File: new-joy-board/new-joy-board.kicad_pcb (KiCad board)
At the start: 2 copper layers, 95.2 x 83.8 mm, 33 parts, among them J0 SDS-50J, J1 SDS-50J, J2 SDS-50J, J3 SDS-50J, J4 BAT, U4 AZReady_ESP32, U5 dc_dc_converter, U6 AZ1117-3.3, U7 MPU6050_Breakout

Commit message: More PCB work to determine final dimensions for case construction
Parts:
- removed C1: 10uF, Capacitor_SMD:C_1210_3225Metric_Pad1.42x2.65mm_HandSolder
- removed C2: 100nF, Capacitor_SMD:C_1210_3225Metric_Pad1.42x2.65mm_HandSolder
- removed U6: AZ1117-3.3, Package_TO_SOT_SMD:SOT-223
- added U0: P82B715, new-joy:P82B715D, F.Cu at (90.2, 144.8)
- added U1: P82B715, new-joy:P82B715D, F.Cu at (90.2, 116.8)
- added U2: P82B715, new-joy:P82B715D, F.Cu at (138.4, 115.6)
- added U3: P82B715, new-joy:P82B715D, F.Cu at (135.9, 146.1)
- moved R9 133.2 mm to (139.5, 154.9)
- moved R10 125.4 mm to (138.4, 136.9), turned to 270 degrees
- moved R5 93.5 mm to (87.0, 123.9)
- moved R11 88.4 mm to (139.5, 123.2)
- moved R12 80.7 mm to (140.8, 106.7)
- moved R4 80.6 mm to (130.6, 106.7)
- moved R13 77.5 mm to (90.0, 106.7)
- moved R14 72.4 mm to (93.8, 125.7)
- moved R6 63.6 mm to (95.0, 109.2)
- moved R2 16.7 mm to (133.1, 137.2)
- moved R3 9.49 mm to (131.1, 123.5)
- moved R1 1.95 mm to (133.3, 155.2), turned to 90 degrees
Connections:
- R10 pad 2: /SDA3ESP -> /SDA3BUF
- U4 pad 1: Net-(U4-Pad1) -> +3V3
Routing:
- net +5V: track 42.3 -> 3.24 mm
- net +3V3: track 27.0 -> 10.7 mm
- net GND: track 7.77 -> 0.00 mm

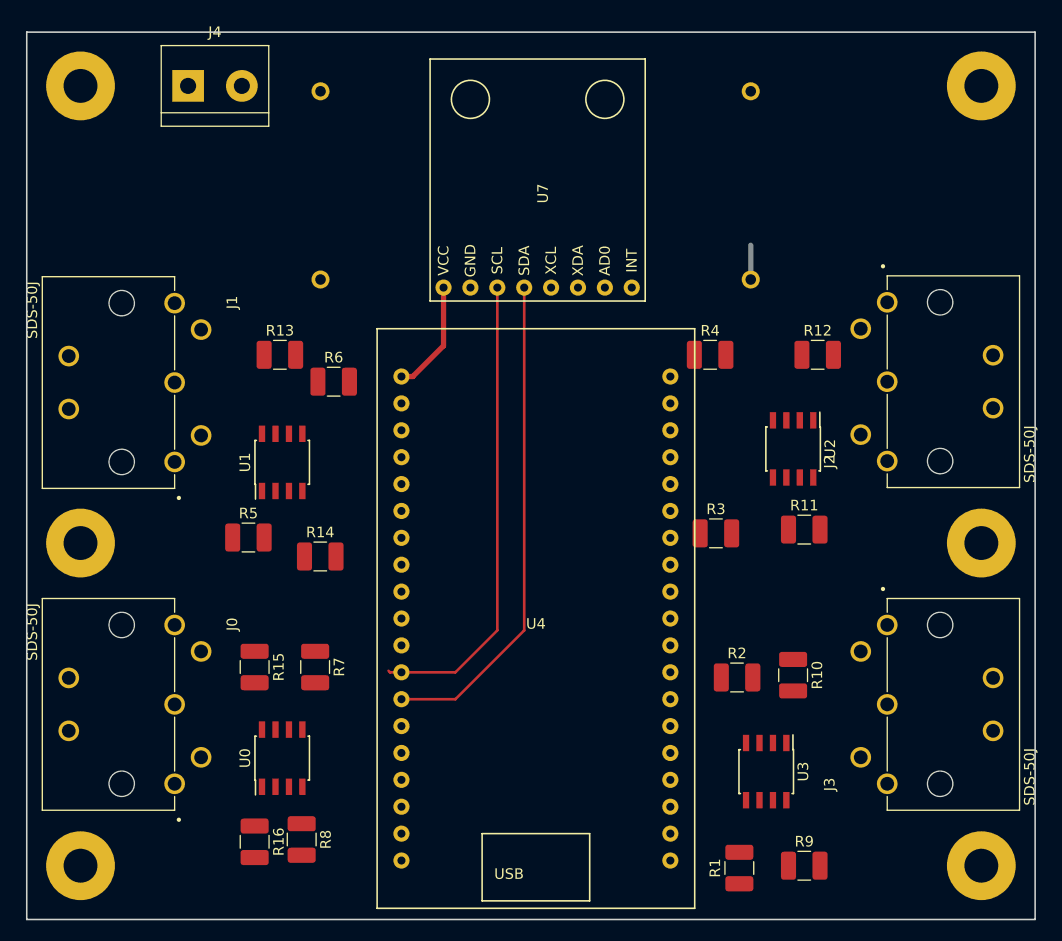
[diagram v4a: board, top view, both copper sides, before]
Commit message: Routet half of the I2C buffers
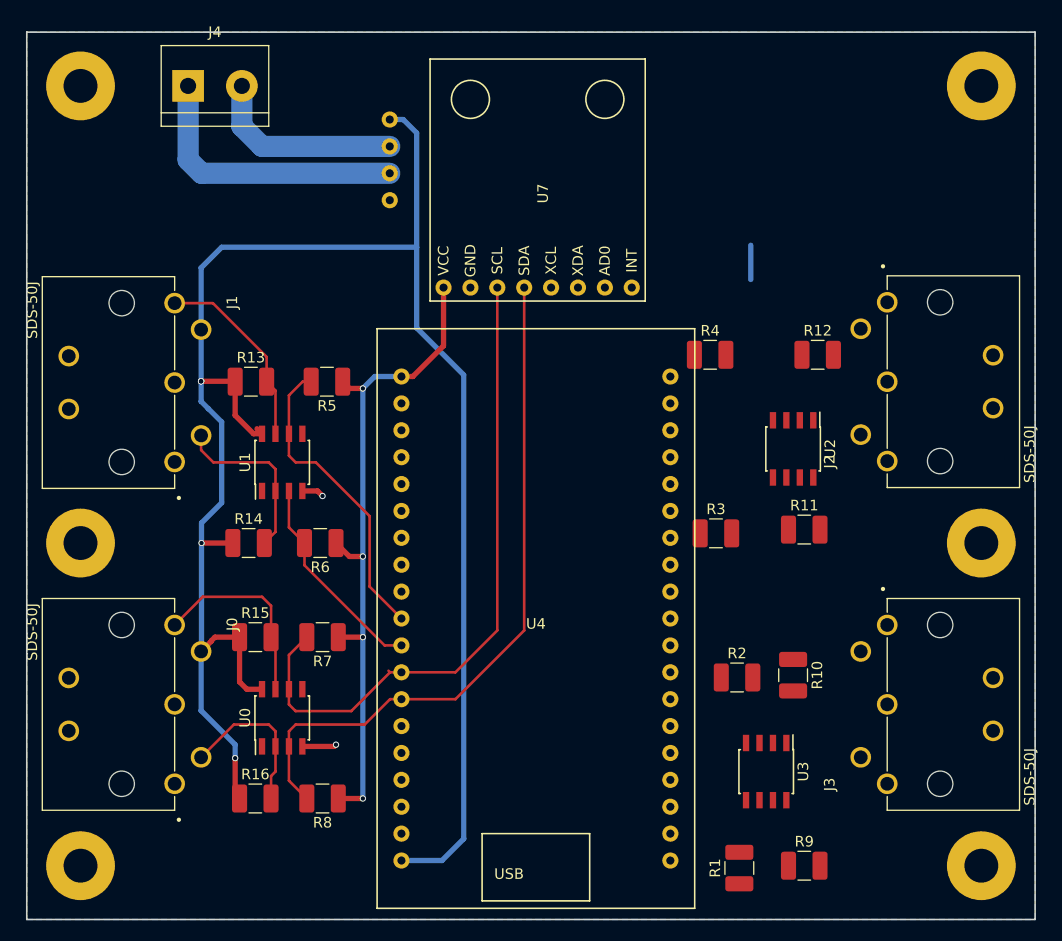
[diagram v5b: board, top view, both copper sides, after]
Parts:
- removed U5: dc_dc_converter, new-joy:dc_dc_converter
- added U10: oskj-dc-dc, new-joy:oskj-dc-dc, B.Cu at (109.2, 88.3)
- moved R5 16.5 mm to (94.4, 109.2), turned to 180 degrees
- moved R6 15.3 mm to (93.8, 124.5), turned to 180 degrees
- moved R14 6.89 mm to (87.0, 124.5)
- moved R8 4.34 mm to (94.0, 148.6), turned to 180 degrees
- moved R16 4.09 mm to (87.6, 148.6), turned to 0 degrees
- moved U0 3.81 mm to (90.2, 141.0)
- moved R13 3.74 mm to (87.2, 109.2)
- moved R7 2.91 mm to (94.0, 133.3), turned to 180 degrees
- moved R15 2.82 mm to (87.6, 133.3), turned to 0 degrees
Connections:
- J0 pad 1: GND -> -BATT
- J1 pad 1: GND -> -BATT
- J2 pad 1: GND -> -BATT
- J3 pad 1: GND -> -BATT
- J4 pad 2: +BATT -> -BATT
- U0 pad 4: GND -> -BATT
- U1 pad 4: GND -> -BATT
- U2 pad 4: GND -> -BATT
- U3 pad 4: GND -> -BATT
- U4 pad 32: GND -> -BATT
- U4 pad 38: GND -> -BATT
- U7 pad 2: GND -> -BATT
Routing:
- net +5V: track 3.24 -> 180.1 mm, vias 0 -> 4
- net +3V3: track 10.7 -> 63.4 mm, vias 0 -> 4
- net /SCL1ESP: track 0.00 -> 29.2 mm
- net +BATT: track 0.00 -> 26.6 mm
- net -BATT: track 0.00 -> 23.9 mm, vias 0 -> 2
- net /SDA1ESP: track 0.00 -> 19.9 mm
- net /SDA0ESP: track 46.7 -> 65.6 mm
- net /SCL0BUF: track 0.00 -> 18.6 mm
- net /SCL1BUF: track 0.00 -> 18.4 mm
- net /SCL0ESP: track 44.4 -> 62.7 mm
- net /SDA1BUF: track 0.00 -> 16.6 mm
- net /SDA0BUF: track 0.00 -> 15.1 mm
- added copper zone on B.Cu, net -BATT

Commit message: First draft of full layout
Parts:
- moved R1 3.39 mm to (133.3, 151.8), turned to 0 degrees
- moved R9 3.18 mm to (139.7, 151.8), turned to 180 degrees
- moved R4 2.83 mm to (133.3, 107.3)
- moved R3 2.42 mm to (133.3, 122.6)
- moved U2 2.01 mm to (136.5, 114.9)
- moved U3 1.86 mm to (136.5, 144.3)
- moved R10 1.29 mm to (139.7, 137.2), turned to 180 degrees
- moved R11 1.06 mm to (140.3, 122.6), turned to 180 degrees
- moved R12 0.76 mm to (140.3, 107.3), turned to 180 degrees
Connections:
- J0 pad S1: Net-(J0-PadS1) -> -BATT
- J0 pad S2: Net-(J0-PadS1) -> -BATT
- J1 pad S1: Net-(J1-PadS1) -> -BATT
- J1 pad S2: Net-(J1-PadS1) -> -BATT
- J2 pad S1: Net-(J2-PadS1) -> -BATT
- J2 pad S2: Net-(J2-PadS1) -> -BATT
- J3 pad S1: Net-(J3-PadS1) -> -BATT
- J3 pad S2: Net-(J3-PadS1) -> -BATT
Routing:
- net +5V: track 180.1 -> 285.5 mm, vias 4 -> 11
- net +3V3: track 63.4 -> 143.7 mm, vias 4 -> 8
- net /SDA2ESP: track 0.00 -> 33.8 mm
- net /SDA2BUF: track 0.00 -> 23.2 mm
- net /SCL2ESP: track 0.00 -> 22.8 mm
- net /SCL2BUF: track 0.00 -> 17.9 mm
- net /SCL3ESP: track 0.00 -> 17.7 mm
- net /SDA3ESP: track 0.00 -> 17.7 mm
- net /SCL3BUF: track 0.00 -> 17.6 mm
- net /SDA3BUF: track 0.00 -> 13.9 mm
- net -BATT: track 23.9 -> 26.5 mm, vias 2 -> 4
- net /SCL1ESP: track 29.2 -> 31.7 mm

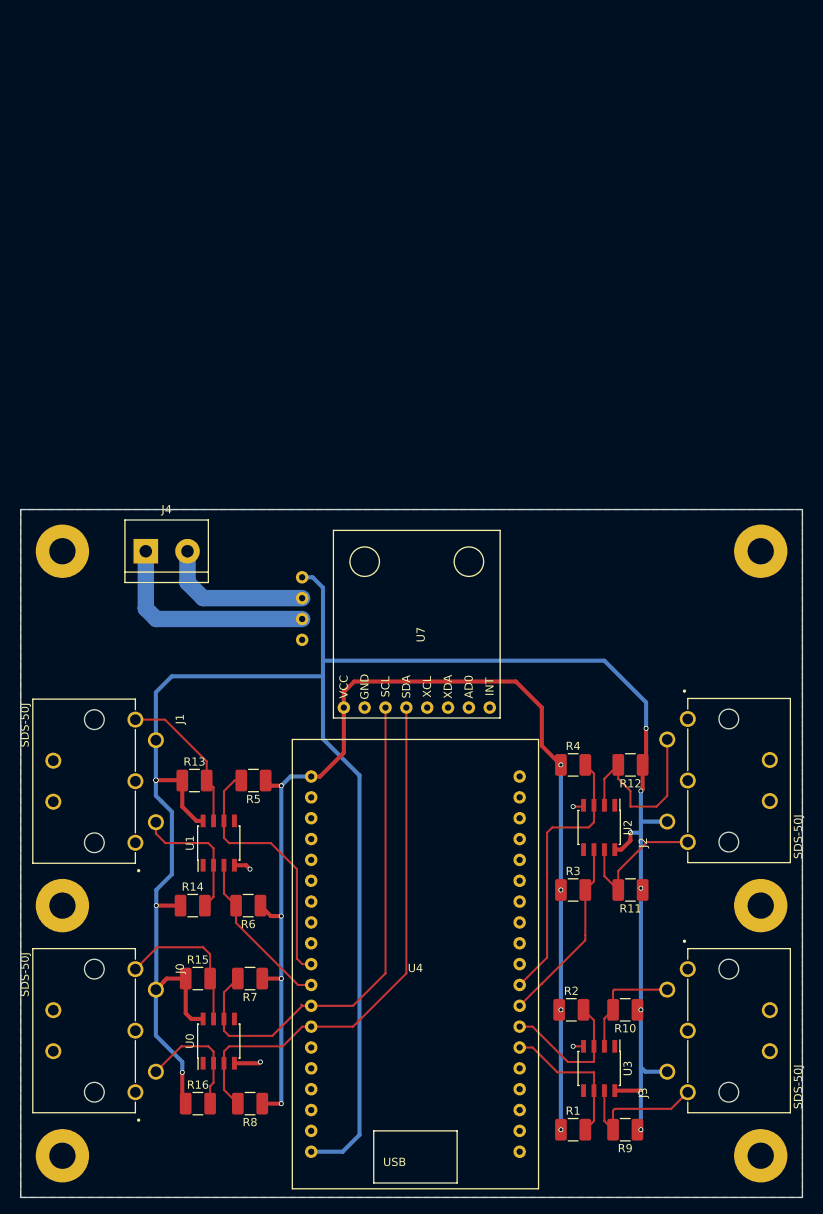
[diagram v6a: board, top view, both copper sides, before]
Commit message: Start rework to slimmer design, and add capacitors to I2C drivers
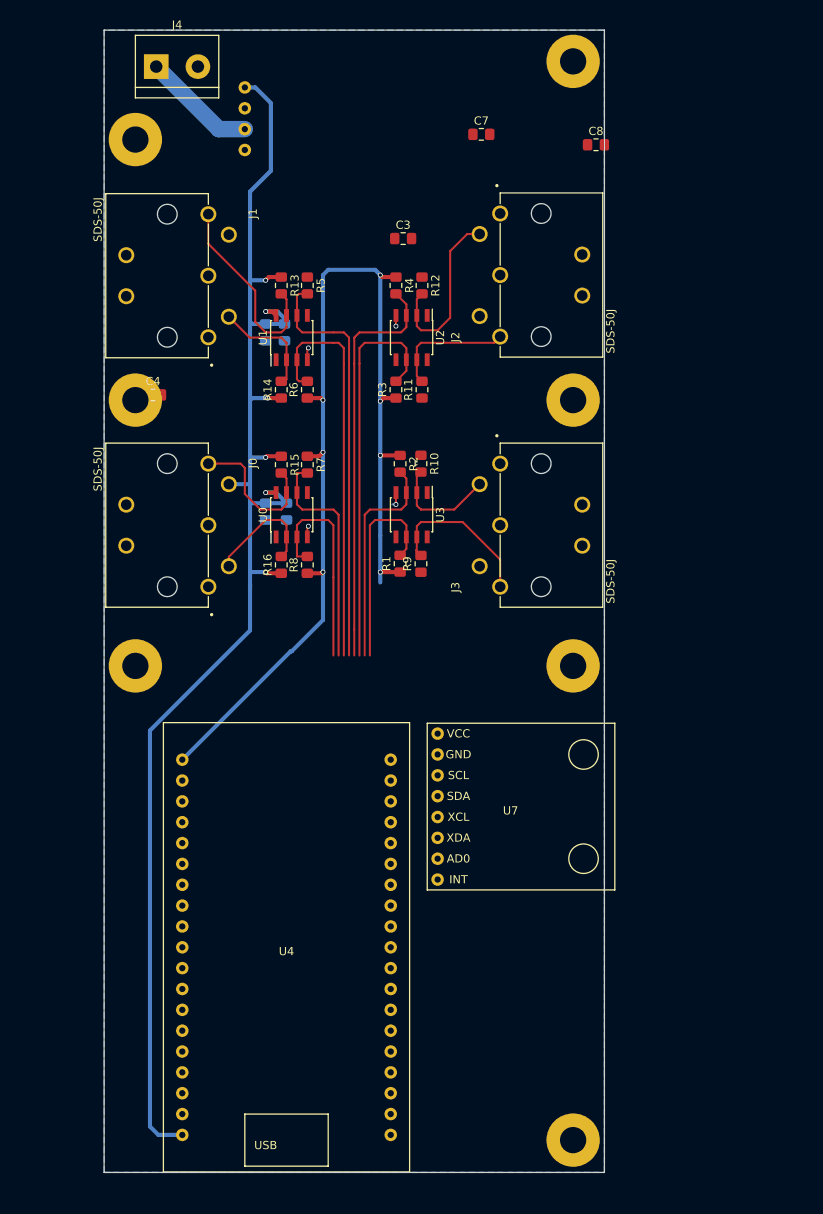
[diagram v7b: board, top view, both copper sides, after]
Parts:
- removed the REF** at (156.2, 81.3)
- removed the REF** at (156.2, 124.5)
- added C1: 0.1uF, Capacitor_SMD:C_0805_2012Metric_Pad1.15x1.40mm_HandSolder, B.Cu at (98.4, 76.4)
- added C2: 0.1uF, Capacitor_SMD:C_0805_2012Metric_Pad1.15x1.40mm_HandSolder, B.Cu at (95.9, 54.6)
- added C3: 0.1uF, Capacitor_SMD:C_0805_2012Metric_Pad1.15x1.40mm_HandSolder, F.Cu at (112.6, 43.2)
- added C4: 0.1uF, Capacitor_SMD:C_0805_2012Metric_Pad1.15x1.40mm_HandSolder, F.Cu at (82.2, 62.2)
- added C5: 1uF, Capacitor_SMD:C_0805_2012Metric_Pad1.15x1.40mm_HandSolder, B.Cu at (95.9, 76.4)
- added C6: 1uF, Capacitor_SMD:C_0805_2012Metric_Pad1.15x1.40mm_HandSolder, B.Cu at (98.2, 54.6)
- added C7: 1uF, Capacitor_SMD:C_0805_2012Metric_Pad1.15x1.40mm_HandSolder, F.Cu at (122.2, 30.5)
- added C8: 1uF, Capacitor_SMD:C_0805_2012Metric_Pad1.15x1.40mm_HandSolder, F.Cu at (136.1, 31.8)
- added REF**: VAL**, new-joy:z_MountPTH_3mm, F.Cu at (133.3, 153.0)
- added REF**: VAL**, new-joy:z_MountPTH_3mm, F.Cu at (133.3, 21.6)
- added REF**: VAL**, new-joy:z_MountPTH_3mm, F.Cu at (133.3, 62.9)
- R1, R10, R11, R12, R13, R14, R15, R16, R2, R3, R4, R5, R6, R7, R8, R9: footprint Resistor_SMD:R_1210_3225Metric_Pad1.42x2.65mm_HandSolder -> Resistor_SMD:R_0805_2012Metric_Pad1.15x1.40mm_HandSolder
- moved R9 73.3 mm to (114.8, 82.8), turned to 90 degrees
- moved R1 72.1 mm to (112.3, 82.8), turned to 90 degrees
- moved U3 71.2 mm to (113.7, 76.8)
- moved R10 71.1 mm to (114.8, 70.6), turned to 270 degrees
- moved R2 69.7 mm to (112.3, 70.6), turned to 270 degrees
- moved R16 66.4 mm to (97.8, 82.9), turned to 90 degrees
- moved R11 66.0 mm to (114.9, 61.6), turned to 90 degrees
- moved R8 66.0 mm to (101.0, 82.9), turned to 90 degrees
- moved J2 65.7 mm to (124.5, 47.6)
- moved J3 65.7 mm to (124.5, 78.1)
- moved U0 64.7 mm to (99.1, 76.8)
- moved R3 64.7 mm to (111.8, 61.6), turned to 90 degrees
- moved U2 63.9 mm to (113.7, 55.2)
- moved REF** 63.9 mm to (133.3, 95.2)
- moved R14 63.8 mm to (97.8, 61.6), turned to 90 degrees
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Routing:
- net +5V: track 285.5 -> 175.7 mm, vias 11 -> 6
- net /SDA0ESP: track 65.6 -> 25.9 mm
- net /SCL0ESP: track 62.7 -> 27.8 mm
- net /SDA1ESP: track 19.9 -> 48.9 mm
- net /SCL2ESP: track 22.8 -> 48.3 mm
- net -BATT: track 26.5 -> 6.02 mm
- net /SCL1ESP: track 31.7 -> 50.8 mm
- net +3V3: track 143.7 -> 126.2 mm, vias 8 -> 7
- net /SDA2ESP: track 33.8 -> 50.2 mm
- net +BATT: track 26.6 -> 14.0 mm
- net /SDA3ESP: track 17.7 -> 27.0 mm
- net /SCL3ESP: track 17.7 -> 24.8 mm
- net /SCL1BUF: track 18.4 -> 24.4 mm
- net /SDA1BUF: track 16.6 -> 13.5 mm
- net /SCL2BUF: track 17.9 -> 15.1 mm
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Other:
- board size 95.2 x 83.8 mm -> 61 x 139.2 mm

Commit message: Route new board layout
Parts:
- C3, C4, C7, C8: moved to B.Cu
- moved C8 50.1 mm to (113.0, 76.2), turned to 90 degrees
- moved C4 36.2 mm to (115.6, 76.2), turned to 90 degrees
- moved C7 25.1 mm to (116.2, 54.9), turned to 90 degrees
- moved C3 11.7 mm to (113.7, 54.9), turned to 90 degrees
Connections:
- U4 pad 10: /SCL1ESP -> /SDA0ESP
- U4 pad 11: /SDA1ESP -> /SCL0ESP
- U4 pad 12: /SCL0ESP -> /SDA1ESP
- U4 pad 13: /SDA0ESP -> /SCL1ESP
- U4 pad 25: /SCL3ESP -> /SDA2ESP
- U4 pad 26: /SDA3ESP -> /SCL2ESP
- U4 pad 27: /SCL2ESP -> /SDA3ESP
- U4 pad 28: /SDA2ESP -> /SCL3ESP
- U7 pad 3: /SCL0ESP -> /SCL3ESP
- U7 pad 4: /SDA0ESP -> /SDA3ESP
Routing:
- net +5V: track 175.7 -> 291.2 mm, vias 6 -> 12
- net /SDA3ESP: track 27.0 -> 94.8 mm
- net /SCL3ESP: track 24.8 -> 89.8 mm
- net /SCL1ESP: track 50.8 -> 101.8 mm
- net /SDA1ESP: track 48.9 -> 97.4 mm
- net /SDA2ESP: track 50.2 -> 97.8 mm
- net /SCL0ESP: track 27.8 -> 73.3 mm
- net /SCL2ESP: track 48.3 -> 93.0 mm
- net /SDA0ESP: track 25.9 -> 68.9 mm
- net +3V3: track 126.2 -> 149.6 mm, vias 7 -> 8
